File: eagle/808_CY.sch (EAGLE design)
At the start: 112 parts, among them IC1 TL071P, IC2 TL071P, IC3 TL071P, IC4 TL072P, Q1 2N3904, Q2 2N3904, Q3 2N3904, Q4 2N3904, Q5 2N3904, Q6 2N3904, Q7 2N3904, Q8 2N3906

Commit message: finishing routes manually
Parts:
- R105*: device TR808clone:R-EU_0207/5V -> TR808clone:R-EU_0309/10
- R126*: device TR808clone:R-EU_0207/5V -> TR808clone:R-EU_0207/7
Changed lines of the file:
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@@
 <part name="R127*" library="TR808clone" deviceset="R-EU_" device="0207/5V" value="82K"/>
 <part name="V346" library="supply1" deviceset="GND" device=""/>
-<part name="R126*" library="TR808clone" deviceset="R-EU_" device="0207/5V" value="22K"/>
+<part name="R126*" library="TR808clone" deviceset="R-EU_" device="0207/7" value="22K"/>
 <part name="C58*" library="TR808clone" deviceset="C-EU" device="3.5MM_PITCH" value="10n"/>
 <part name="R123*" library="TR808clone" deviceset="R-EU_" device="0207/5V" value="100K"/>
@@
 <part name="R58*" library="TR808clone" deviceset="R-EU_" device="0207/7" value="560R"/>
 <part name="R56*" library="TR808clone" deviceset="R-EU_" device="0207/5V" value="560R"/>
-<part name="R105*" library="TR808clone" deviceset="R-EU_" device="0207/5V" value="33K"/>
+<part name="R105*" library="TR808clone" deviceset="R-EU_" device="0309/10" value="33K"/>
 <part name="V33" library="supply1" deviceset="GND" device=""/>
 <part name="R102*" library="TR808clone" deviceset="R-EU_" device="0207/7" value="2M"/>

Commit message: more routes
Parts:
- C47*: device TR808clone:C-EU3.5MM_PITCH -> TR808clone:C-EU050-035X075
- R166*: device TR808clone:R-EU_0207/5V -> TR808clone:R-EU_0207/7
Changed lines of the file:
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@@
 <part name="C36*" library="TR808clone" deviceset="C-EU" device="3.5MM_PITCH" value="1.5n"/>
 <part name="D5*" library="TR808clone" deviceset="1N4148" device="DO35-10" value="1N4148DO35-10"/>
-<part name="C47*" library="TR808clone" deviceset="C-EU" device="3.5MM_PITCH" value="1.5n"/>
+<part name="C47*" library="TR808clone" deviceset="C-EU" device="050-035X075" value="1.5n"/>
 <part name="V329" library="supply1" deviceset="GND" device=""/>
 <part name="V330" library="supply1" deviceset="GND" device=""/>
@@
 <part name="C77*" library="TR808clone" deviceset="C-EU" device="025-025X050" value="220p"/>
 <part name="C78*" library="TR808clone" deviceset="CPOL-EU" device="E2-5" value="33/6.3"/>
-<part name="R166*" library="TR808clone" deviceset="R-EU_" device="0207/5V" value="1K"/>
+<part name="R166*" library="TR808clone" deviceset="R-EU_" device="0207/7" value="1K"/>
 <part name="R118*" library="TR808clone" deviceset="R-EU_" device="0207/5V" value="47K"/>
 <part name="V345" library="supply1" deviceset="GND" device=""/>

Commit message: more routes
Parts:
- C55*: device TR808clone:C-EU3.5MM_PITCH -> TR808clone:C-EU050-030X075
- R109*, R111*, R91*, R93*: device TR808clone:R-EU_0207/5V -> TR808clone:R-EU_0207/7
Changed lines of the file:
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@@
 <part name="V333" library="supply1" deviceset="GND" device=""/>
 <part name="D6*" library="TR808clone" deviceset="1N4148" device="DO35-7"/>
-<part name="R91*" library="TR808clone" deviceset="R-EU_" device="0207/5V" value="33K"/>
+<part name="R91*" library="TR808clone" deviceset="R-EU_" device="0207/7" value="33K"/>
 <part name="R92*" library="TR808clone" deviceset="R-EU_" device="0207/5V" value="33K"/>
 <part name="R89*" library="TR808clone" deviceset="R-EU_" device="0207/5V" value="10K"/>
@@
 <part name="V337" library="supply1" deviceset="GND" device=""/>
 <part name="D8*" library="TR808clone" deviceset="1N4148" device="DO35-7"/>
-<part name="R93*" library="TR808clone" deviceset="R-EU_" device="0207/5V" value="470K"/>
+<part name="R93*" library="TR808clone" deviceset="R-EU_" device="0207/7" value="470K"/>
 <part name="V338" library="supply1" deviceset="GND" device=""/>
 <part name="C54*" library="TR808clone" deviceset="C-EU" device="3.5MM_PITCH" value="1n"/>
@@
 <part name="R106*" library="TR808clone" deviceset="R-EU_" device="0207/5V" value="6K8"/>
 <part name="V339" library="supply1" deviceset="GND" device=""/>
-<part name="R109*" library="TR808clone" deviceset="R-EU_" device="0207/5V" value="18K"/>
+<part name="R109*" library="TR808clone" deviceset="R-EU_" device="0207/7" value="18K"/>
 <part name="V340" library="supply1" deviceset="GND" device=""/>
-<part name="R111*" library="TR808clone" deviceset="R-EU_" device="0207/5V" value="22K"/>
+<part name="R111*" library="TR808clone" deviceset="R-EU_" device="0207/7" value="22K"/>
 <part name="V341" library="supply1" deviceset="GND" device=""/>
 <part name="R110*" library="TR808clone" deviceset="R-EU_" device="0207/7" value="39K"/>
-<part name="C55*" library="TR808clone" deviceset="C-EU" device="3.5MM_PITCH" value="10n"/>
+<part name="C55*" library="TR808clone" deviceset="C-EU" device="050-030X075" value="10n"/>
 <part name="R112*" library="TR808clone" deviceset="R-EU_" device="0207/5V" value="22K"/>
 <part name="R119*" library="TR808clone" deviceset="R-EU_" device="0207/5V" value="22K"/>

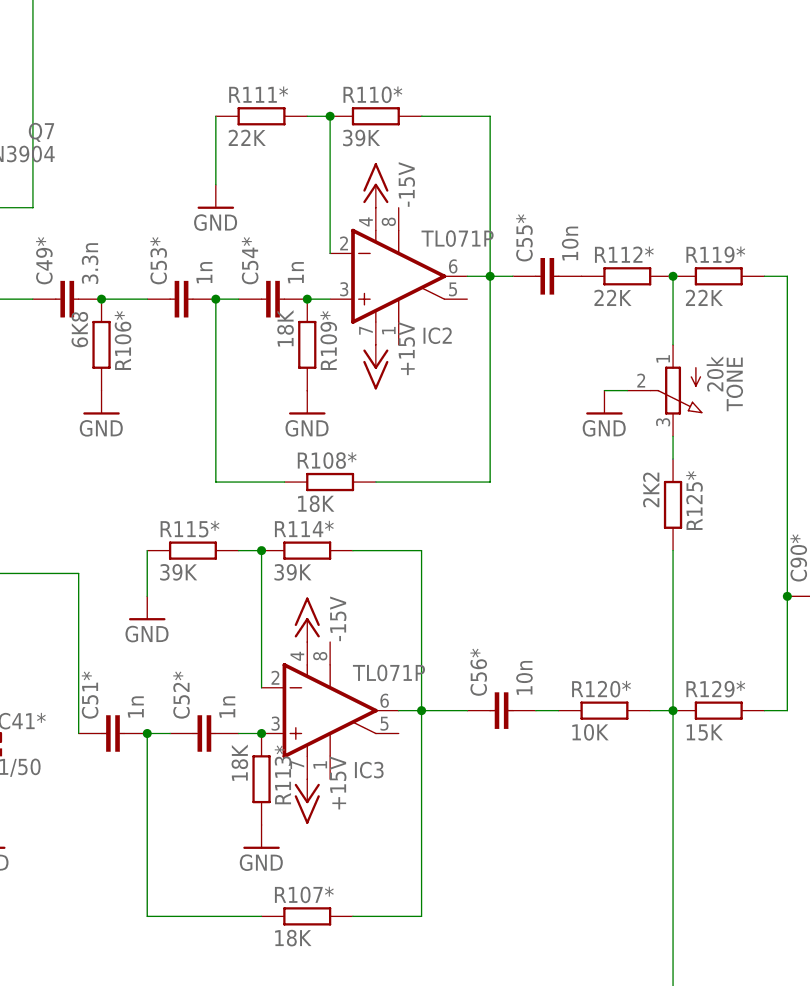
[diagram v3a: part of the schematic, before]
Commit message: ar 94pct with 072 replacing two 071
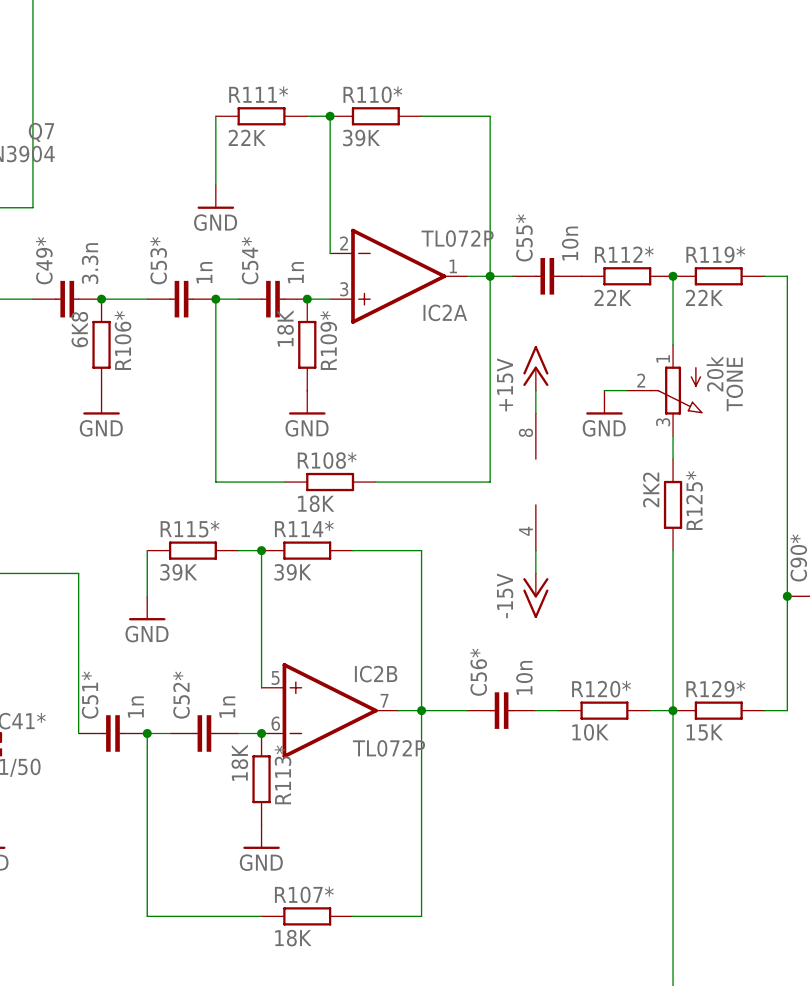
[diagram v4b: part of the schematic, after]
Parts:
- removed IC3: TL071P, linear:TL071P
- IC2: value TL071P -> TL072P; device linear:TL071P -> linear:TL072P
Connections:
- net +15V: now also IC2P.V+; no longer IC2.V+, IC3.V+
- net -15V: now also IC2P.V-; no longer IC2.V-, IC3.V-
- net N$531: now also IC2A.+IN; no longer IC2.+IN
- net N$533: now also IC2A.OUT; no longer IC2.OUT
- net N$535: now also IC2A.-IN; no longer IC2.-IN
- net N$538: now also IC2B.-IN; no longer IC3.+IN
- net N$539: now also IC2B.OUT; no longer IC3.OUT
- net N$541: now also IC2B.+IN; no longer IC3.-IN

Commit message: finishing manually with two 072
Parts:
- R84*: device TR808clone:R-EU_0207/5V -> TR808clone:R-EU_0207/7
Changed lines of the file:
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@@
 <grid distance="0.1" unitdist="inch" unit="inch" style="lines" multiple="1" display="no" altdistance="0.01" altunitdist="inch" altunit="inch"/>
 <layers>
-<layer number="1" name="Top" color="4" fill="1" visible="no" active="no"/>
-<layer number="16" name="Bottom" color="1" fill="1" visible="no" active="no"/>
-<layer number="17" name="Pads" color="2" fill="1" visible="no" active="no"/>
-<layer number="18" name="Vias" color="2" fill="1" visible="no" active="no"/>
-<layer number="19" name="Unrouted" color="6" fill="1" visible="no" active="no"/>
-<layer number="20" name="Dimension" color="15" fill="1" visible="no" active="no"/>
-<layer number="21" name="tPlace" color="7" fill="1" visible="no" active="no"/>
-<layer number="22" name="bPlace" color="7" fill="1" visible="no" active="no"/>
-<layer number="23" name="tOrigins" color="15" fill="1" visible="no" active="no"/>
-<layer number="24" name="bOrigins" color="15" fill="1" visible="no" active="no"/>
-<layer number="25" name="tNames" color="7" fill="1" visible="no" active="no"/>
-<layer number="26" name="bNames" color="7" fill="1" visible="no" active="no"/>
-<layer number="27" name="tValues" color="7" fill="1" visible="no" active="no"/>
-<layer number="28" name="bValues" color="7" fill="1" visible="no" active="no"/>
+<layer number="1" name="Top" color="4" fill="1" visible="yes" active="no"/>
+<layer number="16" name="Bottom" color="1" fill="1" visible="yes" active="no"/>
+<layer number="17" name="Pads" color="2" fill="1" visible="yes" active="no"/>
+<layer number="18" name="Vias" color="2" fill="1" visible="yes" active="no"/>
+<layer number="19" name="Unrouted" color="6" fill="1" visible="yes" active="no"/>
+<layer number="20" name="Dimension" color="15" fill="1" visible="yes" active="no"/>
+<layer number="21" name="tPlace" color="7" fill="1" visible="yes" active="no"/>
+<layer number="22" name="bPlace" color="7" fill="1" visible="yes" active="no"/>
+<layer number="23" name="tOrigins" color="15" fill="1" visible="yes" active="no"/>
+<layer number="24" name="bOrigins" color="15" fill="1" visible="yes" active="no"/>
+<layer number="25" name="tNames" color="7" fill="1" visible="yes" active="no"/>
+<layer number="26" name="bNames" color="7" fill="1" visible="yes" active="no"/>
+<layer number="27" name="tValues" color="7" fill="1" visible="yes" active="no"/>
+<layer number="28" name="bValues" color="7" fill="1" visible="yes" active="no"/>
 <layer number="29" name="tStop" color="7" fill="3" visible="no" active="no"/>
 <layer number="30" name="bStop" color="7" fill="6" visible="no" active="no"/>
@@
 <layer number="35" name="tGlue" color="7" fill="4" visible="no" active="no"/>
 <layer number="36" name="bGlue" color="7" fill="5" visible="no" active="no"/>
-<layer number="37" name="tTest" color="7" fill="1" visible="no" active="no"/>
-<layer number="38" name="bTest" color="7" fill="1" visible="no" active="no"/>
+<layer number="37" name="tTest" color="7" fill="1" visible="yes" active="no"/>
+<layer number="38" name="bTest" color="7" fill="1" visible="yes" active="no"/>
 <layer number="39" name="tKeepout" color="4" fill="11" visible="no" active="no"/>
 <layer number="40" name="bKeepout" color="1" fill="11" visible="no" active="no"/>
@@
 <layer number="44" name="Drills" color="7" fill="1" visible="no" active="no"/>
 <layer number="45" name="Holes" color="7" fill="1" visible="no" active="no"/>
-<layer number="46" name="Milling" color="3" fill="1" visible="no" active="no"/>
-<layer number="47" name="Measures" color="7" fill="1" visible="no" active="no"/>
-<layer number="48" name="Document" color="7" fill="1" visible="no" active="no"/>
-<layer number="49" name="Reference" color="7" fill="1" visible="no" active="no"/>
-<layer number="50" name="dxf" color="7" fill="1" visible="no" active="no"/>
-<layer number="51" name="tDocu" color="7" fill="1" visible="no" active="no"/>
-<layer number="52" name="bDocu" color="7" fill="1" visible="no" active="no"/>
-<layer number="53" name="tGND_GNDA" color="7" fill="9" visible="no" active="no"/>
-<layer number="54" name="bGND_GNDA" color="1" fill="9" visible="no" active="no"/>
-<layer number="56" name="wert" color="7" fill="1" visible="no" active="no"/>
-<layer number="57" name="tCAD" color="7" fill="1" visible="no" active="no"/>
-<layer number="59" name="tCarbon" color="7" fill="1" visible="no" active="no"/>
-<layer number="60" name="bCarbon" color="7" fill="1" visible="no" active="no"/>
+<layer number="46" name="Milling" color="3" fill="1" visible="yes" active="no"/>
+<layer number="47" name="Measures" color="7" fill="1" visible="yes" active="no"/>
+<layer number="48" name="Document" color="7" fill="1" visible="yes" active="no"/>
+<layer number="49" name="Reference" color="7" fill="1" visible="yes" active="no"/>
+<layer number="50" name="dxf" color="7" fill="1" visible="yes" active="no"/>
+<layer number="51" name="tDocu" color="7" fill="1" visible="yes" active="no"/>
+<layer number="52" name="bDocu" color="7" fill="1" visible="yes" active="no"/>
+<layer number="53" name="tGND_GNDA" color="7" fill="9" visible="yes" active="no"/>
+<layer number="54" name="bGND_GNDA" color="1" fill="9" visible="yes" active="no"/>
+<layer number="56" name="wert" color="7" fill="1" visible="yes" active="no"/>
+<layer number="57" name="tCAD" color="7" fill="1" visible="yes" active="no"/>
+<layer number="59" name="tCarbon" color="7" fill="1" visible="yes" active="no"/>
+<layer number="60" name="bCarbon" color="7" fill="1" visible="yes" active="no"/>
 <layer number="90" name="Modules" color="5" fill="1" visible="yes" active="yes"/>
 <layer number="91" name="Nets" color="2" fill="1" visible="yes" active="yes"/>
@@
 <part name="R86*" library="TR808clone" deviceset="R-EU_" device="0207/7" value="100R"/>
 <part name="R85*" library="TR808clone" deviceset="R-EU_" device="0207/5V" value="100R"/>
-<part name="R84*" library="TR808clone" deviceset="R-EU_" device="0207/5V" value="10K"/>
+<part name="R84*" library="TR808clone" deviceset="R-EU_" device="0207/7" value="10K"/>
 <part name="R83*" library="TR808clone" deviceset="R-EU_" device="0207/5V" value="22K"/>
 <part name="V325" library="supply1" deviceset="GND" device=""/>

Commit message: more manual routes
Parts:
- R121*, R85*, R98*: device TR808clone:R-EU_0207/5V -> TR808clone:R-EU_0207/7
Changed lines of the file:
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@@
 <part name="C44*" library="TR808clone" deviceset="C-EU" device="050-024X044" value="22n"/>
 <part name="V314" library="supply1" deviceset="GND" device=""/>
-<part name="R98*" library="TR808clone" deviceset="R-EU_" device="0207/5V" value="100R"/>
+<part name="R98*" library="TR808clone" deviceset="R-EU_" device="0207/7" value="100R"/>
 <part name="C43*" library="TR808clone" deviceset="C-EU" device="3.5MM_PITCH" value="1.5n"/>
 <part name="D11*" library="TR808clone" deviceset="1N4148" device="DO35-7"/>
@@
 <part name="V324" library="supply1" deviceset="GND" device=""/>
 <part name="R86*" library="TR808clone" deviceset="R-EU_" device="0207/7" value="100R"/>
-<part name="R85*" library="TR808clone" deviceset="R-EU_" device="0207/5V" value="100R"/>
+<part name="R85*" library="TR808clone" deviceset="R-EU_" device="0207/7" value="100R"/>
 <part name="R84*" library="TR808clone" deviceset="R-EU_" device="0207/7" value="10K"/>
 <part name="R83*" library="TR808clone" deviceset="R-EU_" device="0207/5V" value="22K"/>
@@
 <part name="R123*" library="TR808clone" deviceset="R-EU_" device="0207/5V" value="100K"/>
 <part name="C57*" library="TR808clone" deviceset="C-EU" device="3.5MM_PITCH" value="3.3n"/>
-<part name="R121*" library="TR808clone" deviceset="R-EU_" device="0207/5V" value="10K"/>
+<part name="R121*" library="TR808clone" deviceset="R-EU_" device="0207/7" value="10K"/>
 <part name="V349" library="supply1" deviceset="GND" device=""/>
 <part name="R58*" library="TR808clone" deviceset="R-EU_" device="0207/7" value="560R"/>

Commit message: routed and tweaked
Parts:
- C41*: device TR808clone:CPOL-EUE2.5-5 -> TR808clone:CPOL-EUE3.5-8
- R123*, R89*, R92*: device TR808clone:R-EU_0207/5V -> TR808clone:R-EU_0207/7
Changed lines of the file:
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@@
 <part name="D6*" library="TR808clone" deviceset="1N4148" device="DO35-7"/>
 <part name="R91*" library="TR808clone" deviceset="R-EU_" device="0207/7" value="33K"/>
-<part name="R92*" library="TR808clone" deviceset="R-EU_" device="0207/5V" value="33K"/>
-<part name="R89*" library="TR808clone" deviceset="R-EU_" device="0207/5V" value="10K"/>
+<part name="R92*" library="TR808clone" deviceset="R-EU_" device="0207/7" value="33K"/>
+<part name="R89*" library="TR808clone" deviceset="R-EU_" device="0207/7" value="10K"/>
 <part name="V335" library="supply1" deviceset="GND" device=""/>
-<part name="C41*" library="TR808clone" deviceset="CPOL-EU" device="E2.5-5" value="1/50"/>
+<part name="C41*" library="TR808clone" deviceset="CPOL-EU" device="E3.5-8" value="1/50"/>
 <part name="V337" library="supply1" deviceset="GND" device=""/>
 <part name="D8*" library="TR808clone" deviceset="1N4148" device="DO35-7"/>
@@
 <part name="R126*" library="TR808clone" deviceset="R-EU_" device="0207/7" value="22K"/>
 <part name="C58*" library="TR808clone" deviceset="C-EU" device="3.5MM_PITCH" value="10n"/>
-<part name="R123*" library="TR808clone" deviceset="R-EU_" device="0207/5V" value="100K"/>
+<part name="R123*" library="TR808clone" deviceset="R-EU_" device="0207/7" value="100K"/>
 <part name="C57*" library="TR808clone" deviceset="C-EU" device="3.5MM_PITCH" value="3.3n"/>
 <part name="R121*" library="TR808clone" deviceset="R-EU_" device="0207/7" value="10K"/>
